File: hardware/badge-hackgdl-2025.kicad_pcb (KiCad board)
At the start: 11 copper layers, 73.4 x 79.5 mm, 53 parts, among them J1 ADDON, J2 Battery, P1 USB_C_Plug_USB2.0, Q1 DMG3415U-7, Q2 MMBT2222A, SW1 ON, SW2 RESET, SW3 BOOT, SW4 LEFT, SW5 BACK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

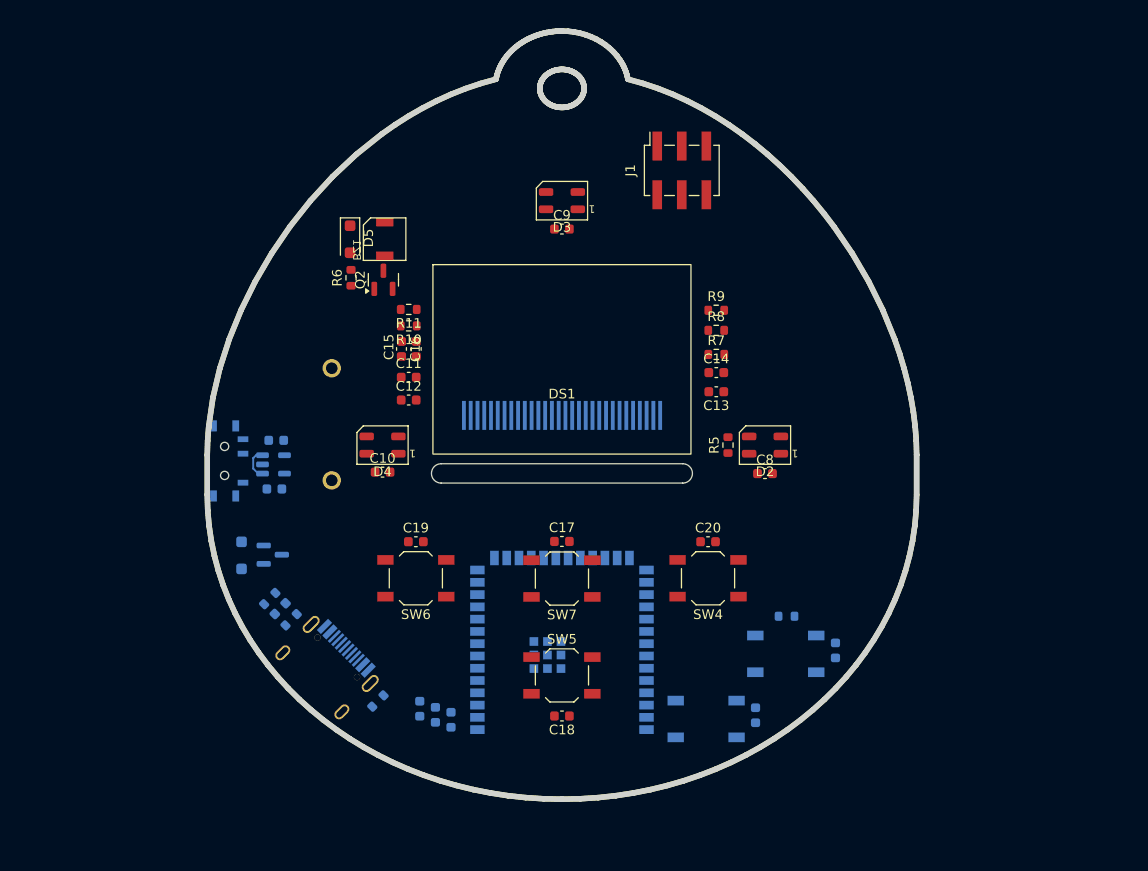
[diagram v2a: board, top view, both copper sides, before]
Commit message: feat(hw): add routes in pcb
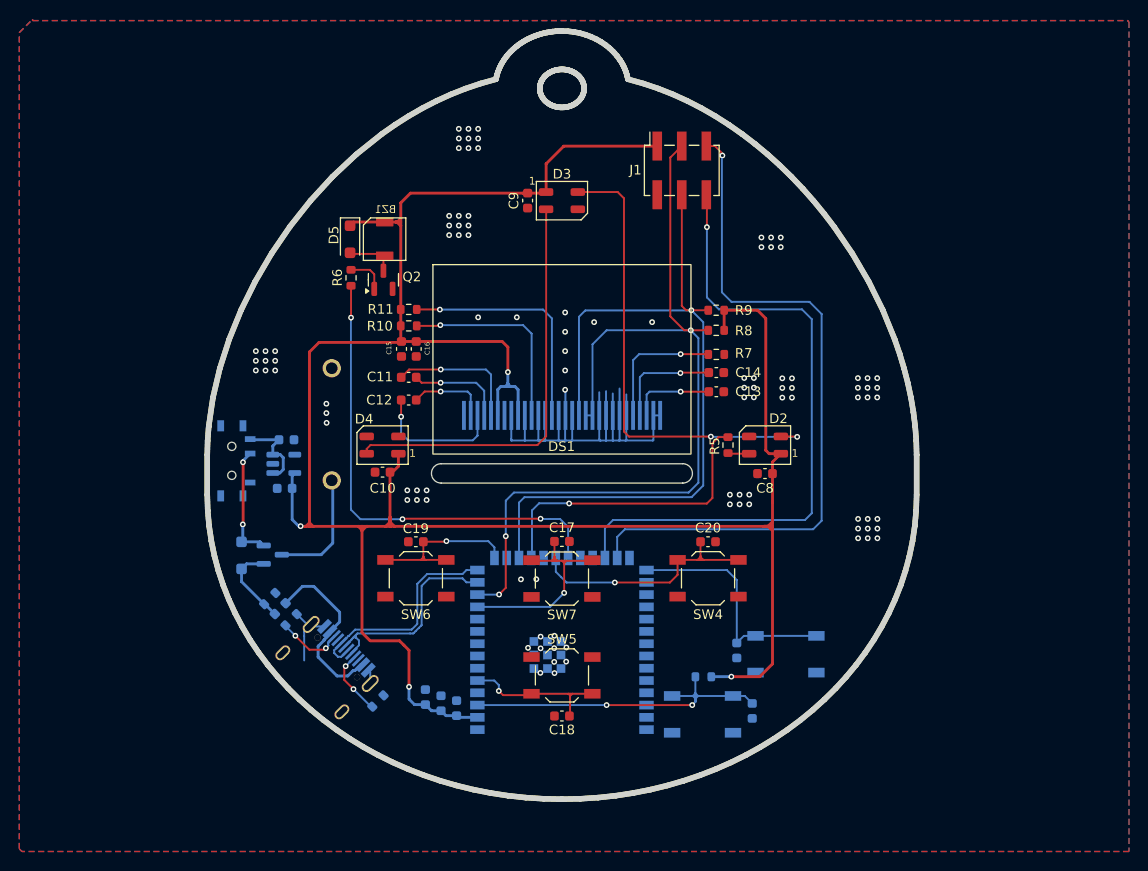
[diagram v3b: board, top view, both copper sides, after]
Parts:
- SW4: value LEFT -> RIGHT
- SW6: value RIGHT -> LEFT
- moved SW2 10.6 mm to (148.2, 89.6)
- moved C6 10.6 mm to (153.4, 89.2)
- moved R4 10.6 mm to (148.3, 85.7)
- moved SW3 10.6 mm to (156.8, 83.4), turned to 0 degrees
- moved C7 6.98 mm to (151.8, 83.0), turned to -90 degrees
- moved C9 4.62 mm to (130.1, 36.4), turned to 90 degrees
- moved C3 1.33 mm to (119.5, 87.8)
- moved C5 1.33 mm to (122.8, 88.9)
- moved C4 1.33 mm to (121.2, 88.4)
- moved C2 1.07 mm to (105.0, 66.2)
- moved U1 1.07 mm to (104.9, 63.7)
- moved C1 1.07 mm to (105.2, 61.2)
- moved SW1 0.75 mm to (99.5, 63.4)
- turned C19 to 180 degrees
- turned D3 to 0 degrees
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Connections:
- C19 pad 1: /RIGHT -> /LEFT
- C20 pad 1: /LEFT -> /RIGHT
- SW4 pad 2: /LEFT -> /RIGHT
- SW6 pad 2: /RIGHT -> /LEFT
- U2 pad 10: /LEFT -> unconnected-(U2-IO17-Pad10)
- U2 pad 11: /BACK -> /MIDDLE
- U2 pad 15: unconnected-(U2-IO3-Pad15) -> /LEFT
- U2 pad 20: unconnected-(U2-IO12-Pad20) -> /RIGHT
- U2 pad 24: unconnected-(U2-IO47-Pad24) -> /GPIO2
- U2 pad 25: unconnected-(U2-IO48-Pad25) -> /GPIO1
- U2 pad 5: unconnected-(U2-IO5-Pad5) -> /BACK
- U2 pad 6: /GPIO1 -> unconnected-(U2-IO6-Pad6)
- U2 pad 7: /GPIO2 -> unconnected-(U2-IO7-Pad7)
- U2 pad 8: /MIDDLE -> unconnected-(U2-IO15-Pad8)
- U2 pad 9: /RIGHT -> unconnected-(U2-IO16-Pad9)
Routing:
- net +3V3: track 0.00 -> 253.9 mm, vias 0 -> 4
- net /SDA: track 0.00 -> 90.5 mm, vias 0 -> 3
- net /SCL: track 0.00 -> 80.7 mm, vias 0 -> 1
- net GND: track 0.00 -> 73.7 mm, vias 0 -> 99
- net /GPIO1: track 0.00 -> 73.0 mm, vias 0 -> 1
- net /GPIO2: track 0.00 -> 67.6 mm, vias 0 -> 1
- net /Buzz: track 0.00 -> 49.6 mm, vias 0 -> 3
- net Net-(D2-DOUT): track 0.00 -> 49.0 mm, vias 0 -> 2
- net Net-(D3-DOUT): track 0.00 -> 43.1 mm
- net /RST: track 0.00 -> 36.2 mm, vias 0 -> 2
- net /NEOPIXEL: track 0.00 -> 31.7 mm, vias 0 -> 1
- net /RIGHT: track 0.00 -> 25.5 mm, vias 0 -> 1
- net /BOOT: track 0.00 -> 24.8 mm
- net Net-(DS1-~{RES}): track 0.00 -> 24.4 mm, vias 0 -> 1
- net /MIDDLE: track 0.00 -> 23.0 mm, vias 0 -> 1
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- added copper zone on B.Cu, net GND
- added copper zone on F.Cu, net GND

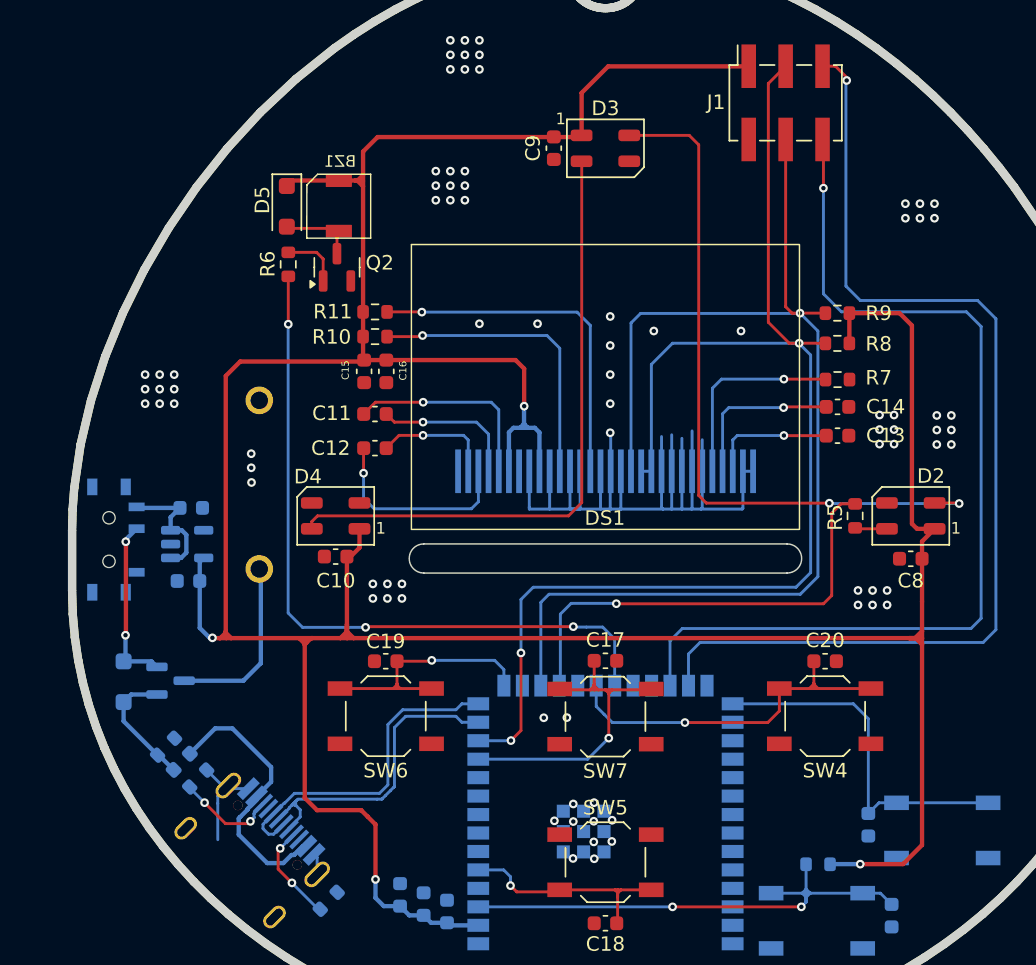
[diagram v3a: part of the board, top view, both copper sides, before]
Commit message: feat(hw): change ON/OFF switch
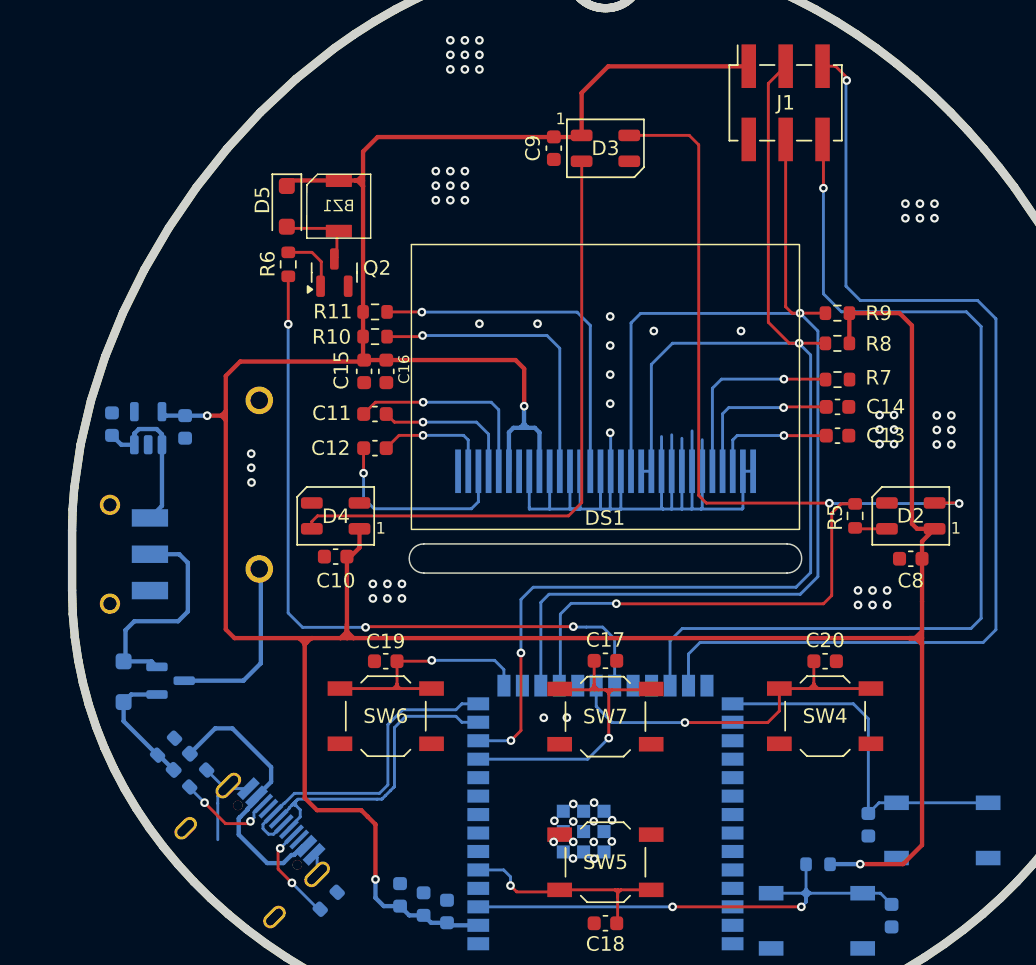
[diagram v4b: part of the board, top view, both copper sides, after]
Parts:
- SW1: footprint Footprints:MSK12C02 -> Footprints:JS102011SAQN
- moved C2 10.6 mm to (104.8, 55.6), turned to -90 degrees
- moved U1 8.41 mm to (102.2, 55.7), turned to 90 degrees
- moved C1 7.93 mm to (99.7, 55.4), turned to 90 degrees
- moved SW1 2.08 mm to (101.3, 64.4)
- moved Q2 0.40 mm to (115.0, 45.0)
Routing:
- net Net-(D1-K): track 12.0 -> 15.7 mm, vias 2 -> 0
- net +3V3: track 253.9 -> 251.1 mm
- net Net-(SW1-A): track 8.49 -> 10.9 mm
- net GND: vias 99 -> 92

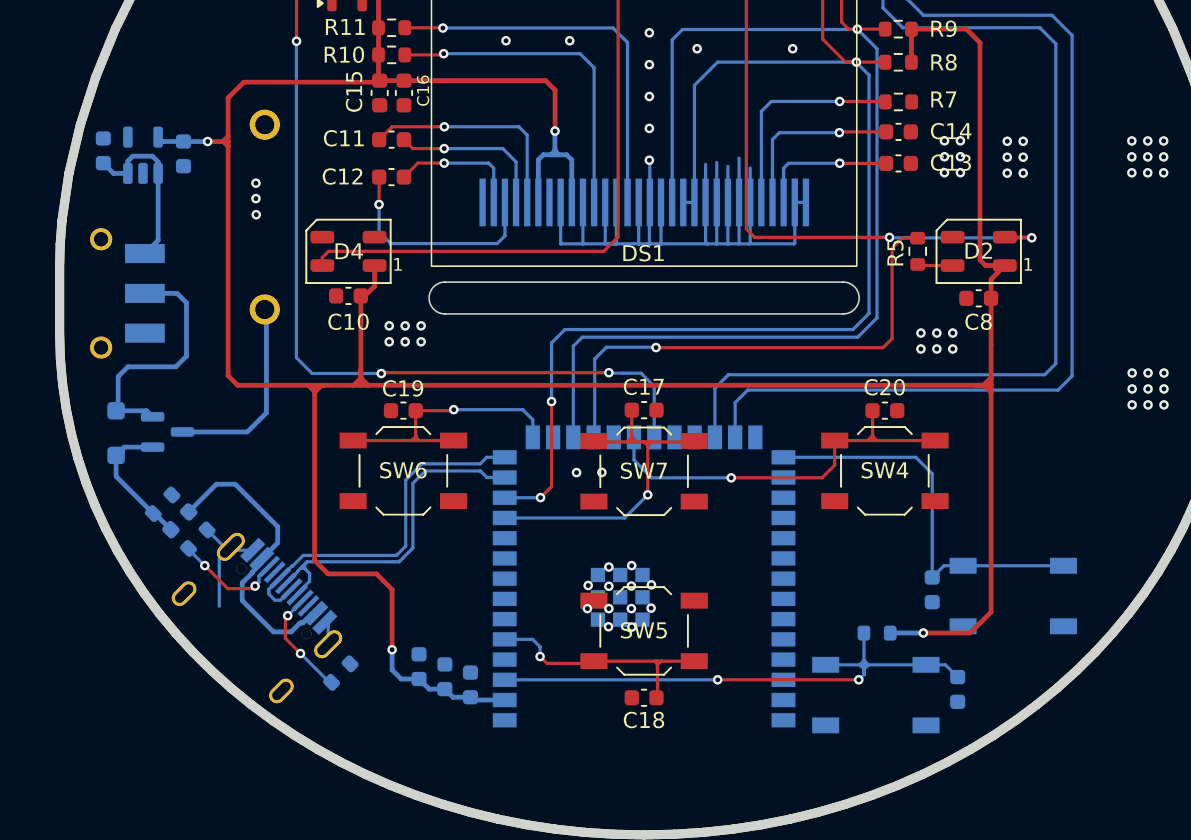
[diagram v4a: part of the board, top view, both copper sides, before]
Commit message: feat(hw): add labels
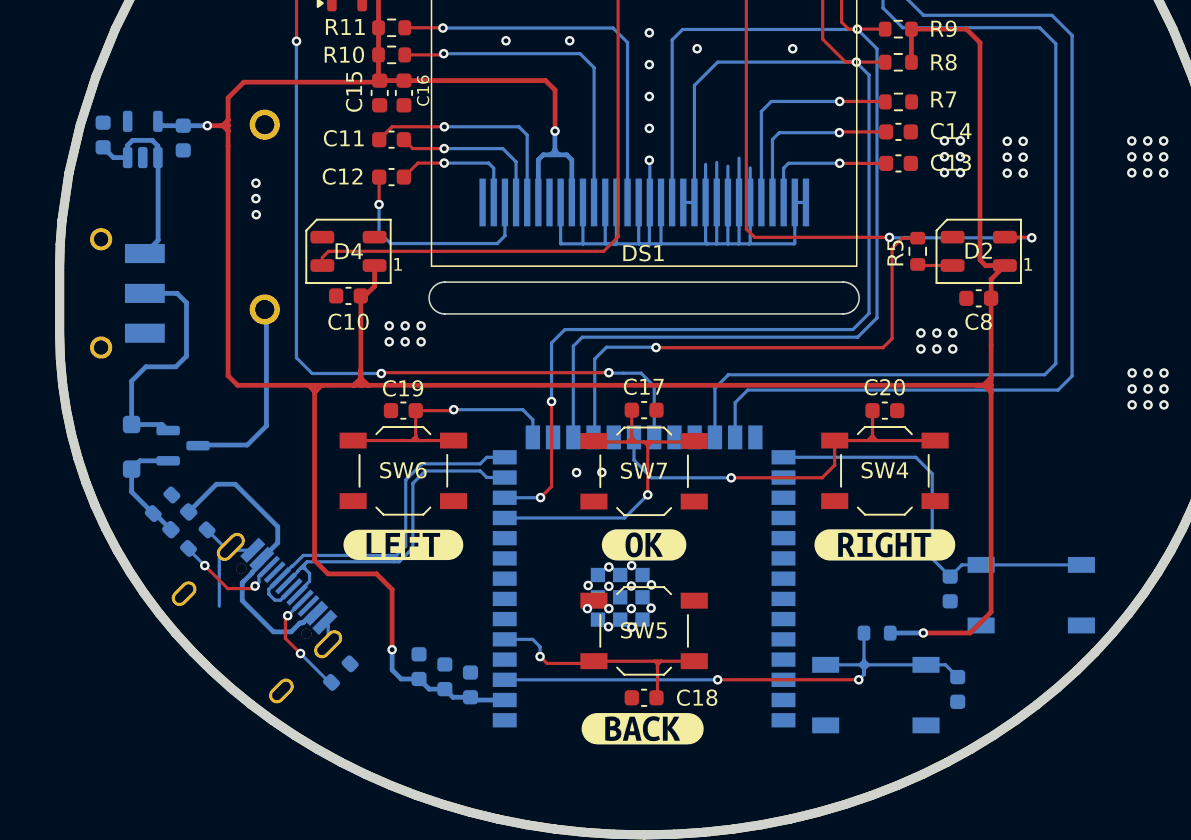
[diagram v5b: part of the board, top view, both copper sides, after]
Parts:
- added kibuzzard-67869934: G***, kibuzzard-67869934, B.Cu at (100.9, 58.5)
- added kibuzzard-67869944: G***, kibuzzard-67869944, B.Cu at (100.9, 70.2)
- added kibuzzard-678699AD: G***, kibuzzard-678699AD, B.Cu at (148.2, 83.9)
- added kibuzzard-678699B2: G***, kibuzzard-678699B2, B.Cu at (158.0, 79.3)
- added kibuzzard-6786EBF3: G***, kibuzzard-6786EBF3, F.Cu at (118.6, 80.2)
- added kibuzzard-6786EC12: G***, kibuzzard-6786EC12, F.Cu at (148.8, 80.2)
- added kibuzzard-6786EC27: G***, kibuzzard-6786EC27, F.Cu at (133.6, 91.7)
- added kibuzzard-6786EC60: G***, kibuzzard-6786EC60, F.Cu at (133.7, 80.2)
- moved D1 1.30 mm to (101.5, 74.0)
- moved Q1 1.30 mm to (104.7, 73.9)
- moved C7 1.13 mm to (152.9, 82.9)
- moved SW3 1.13 mm to (158.0, 83.3)
- moved U1 0.99 mm to (102.2, 54.7)
- moved C1 0.99 mm to (99.7, 54.4)
- moved C2 0.99 mm to (104.7, 54.6)
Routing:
- net VBUS: track 8.66 -> 7.39 mm
- net Net-(SW1-A): track 10.9 -> 11.8 mm

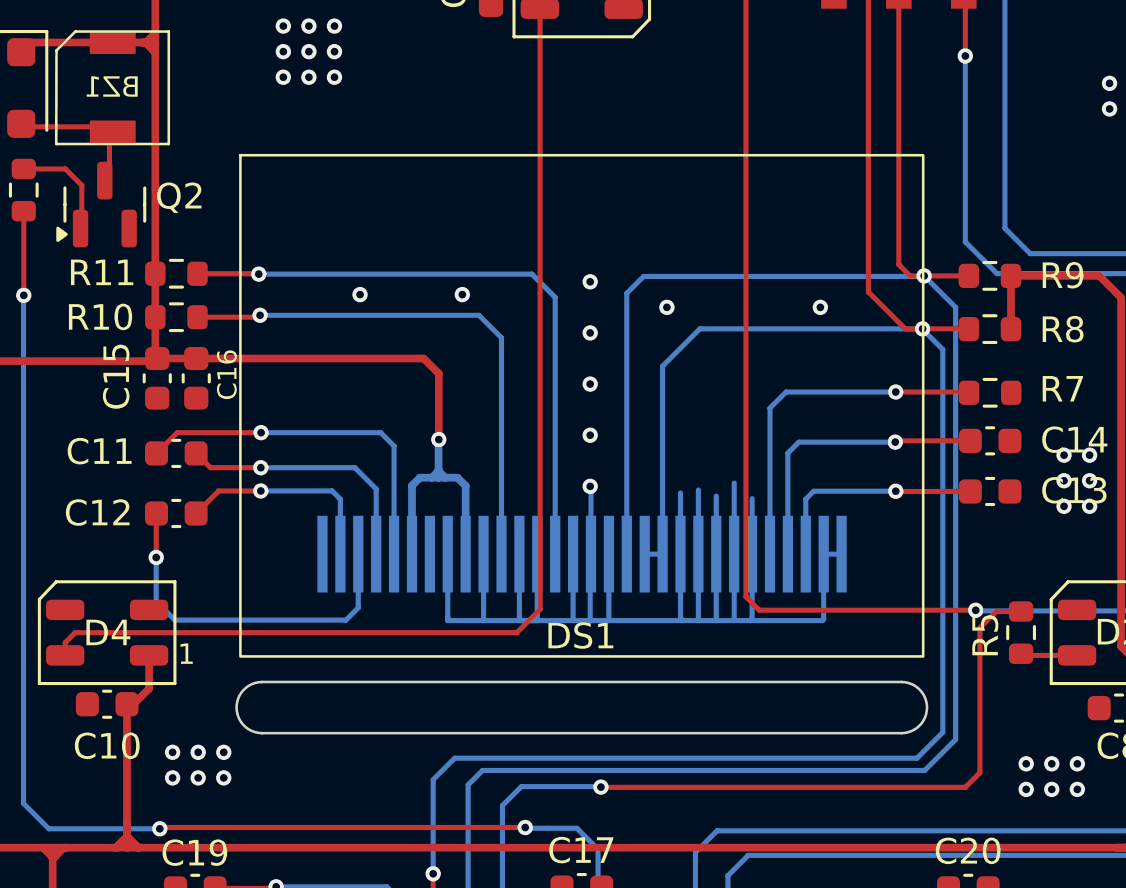
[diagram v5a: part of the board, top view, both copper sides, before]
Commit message: feat(hw): change size of pads in the oled footprint
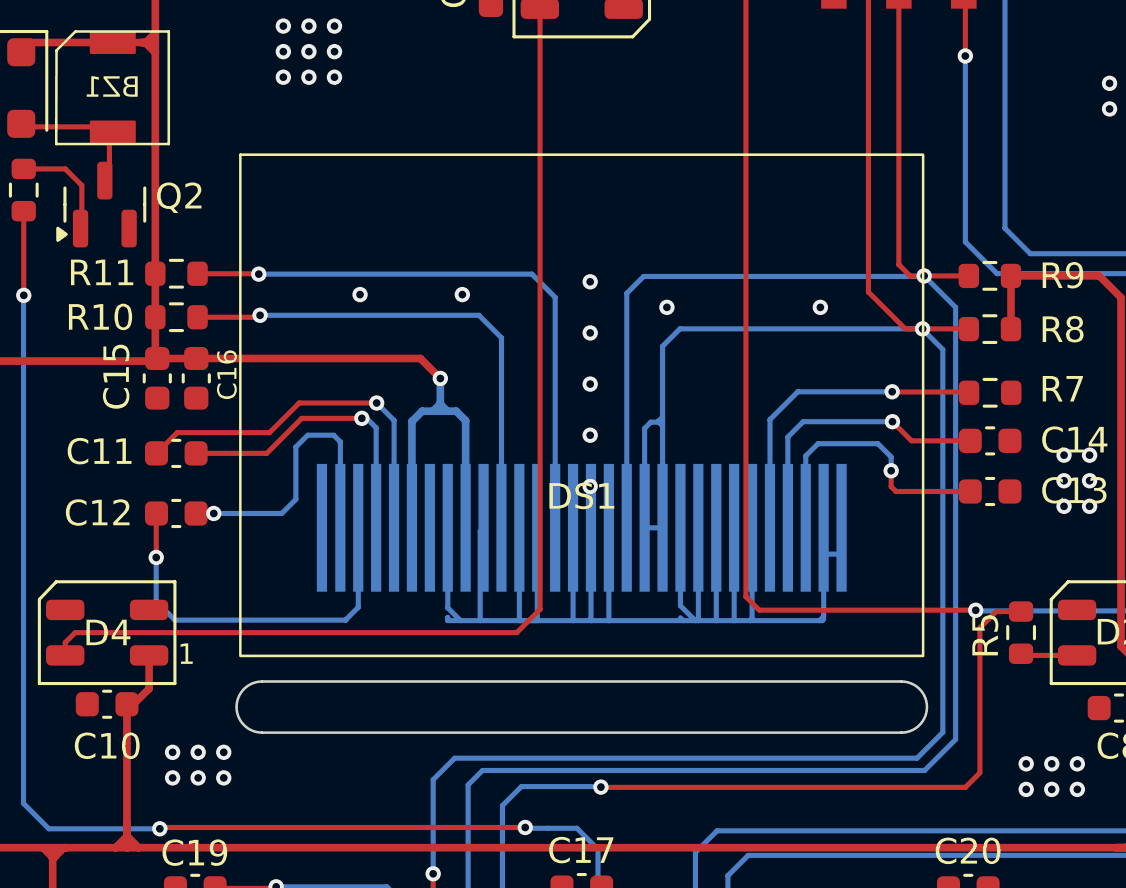
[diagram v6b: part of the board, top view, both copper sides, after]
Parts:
- F1: value 0.5A -> 1A
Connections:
- U2 pad 36: /RXD -> unconnected-(U2-RXD0-Pad36)
- U2 pad 37: /TXD -> unconnected-(U2-TXD0-Pad37)
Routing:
- net /SDA: track 90.5 -> 95.1 mm
- net Net-(DS1-C2N): track 8.29 -> 11.6 mm
- net Net-(DS1-VCC): track 8.72 -> 10.9 mm
- net Net-(DS1-C1P): track 10.2 -> 11.7 mm
- net Net-(DS1-IREF): track 13.8 -> 12.5 mm
- net /SCL: track 80.7 -> 79.7 mm
- net Net-(DS1-~{RES}): track 24.4 -> 23.4 mm
- net Net-(DS1-BS1): track 20.7 -> 19.7 mm
- net Net-(DS1-C2P): track 14.0 -> 15.0 mm
- net Net-(DS1-C1N): track 14.1 -> 14.6 mm
